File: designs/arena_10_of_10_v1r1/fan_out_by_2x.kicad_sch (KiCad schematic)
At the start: 6 parts

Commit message: Added initial annotation.
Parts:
- gave numbers to parts that had none: 4

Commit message: Finished footprint assignment.
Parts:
- R48, R49: footprint (none) -> Resistor_SMD:R_0402_1005Metric
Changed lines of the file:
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@@
 			)
 		)
-		(property "Footprint" ""
+		(property "Footprint" "Resistor_SMD:R_0402_1005Metric"
 			(at 100.33 43.18 0)
 			(effects
@@
 			)
 		)
-		(property "Footprint" ""
+		(property "Footprint" "Resistor_SMD:R_0402_1005Metric"
 			(at 100.33 59.69 0)
 			(effects

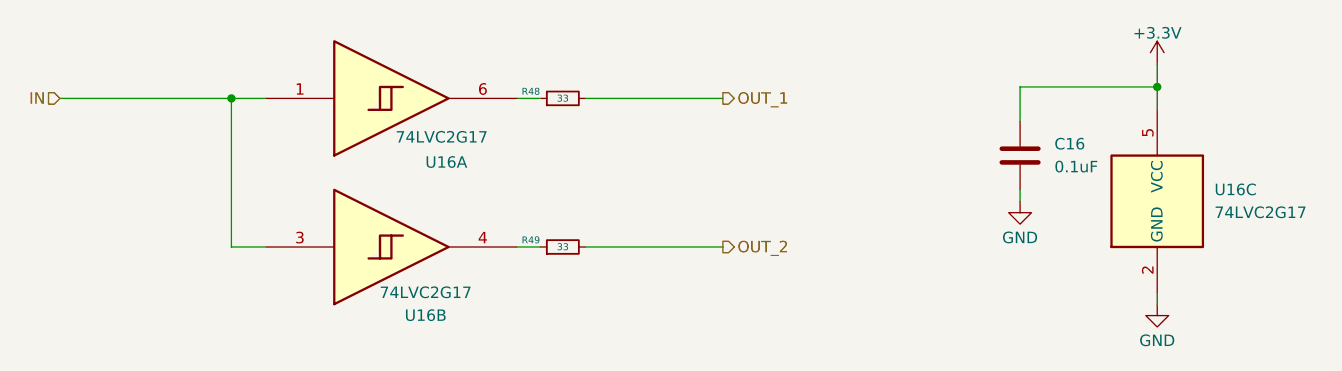
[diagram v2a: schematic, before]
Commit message: Resolved all DSR voilations in schematic.
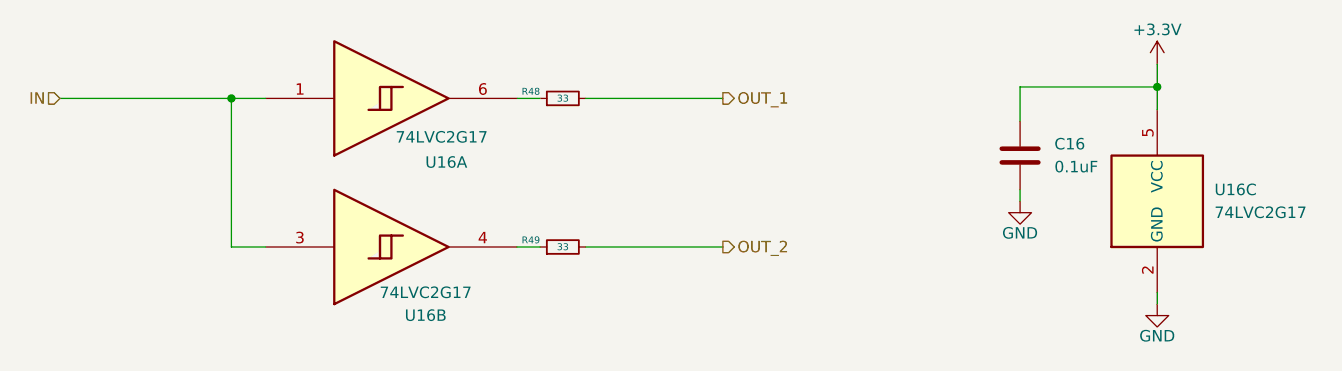
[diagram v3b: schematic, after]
